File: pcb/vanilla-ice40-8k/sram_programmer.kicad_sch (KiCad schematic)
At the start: 43 parts, among them J10 Conn_01x05_Pin, J9 Conn_01x06_Pin, U2 W25X40CLSN, U3 FT2232HL, U4 93LCxxBxxOT, Y1 12Mhz/18pf

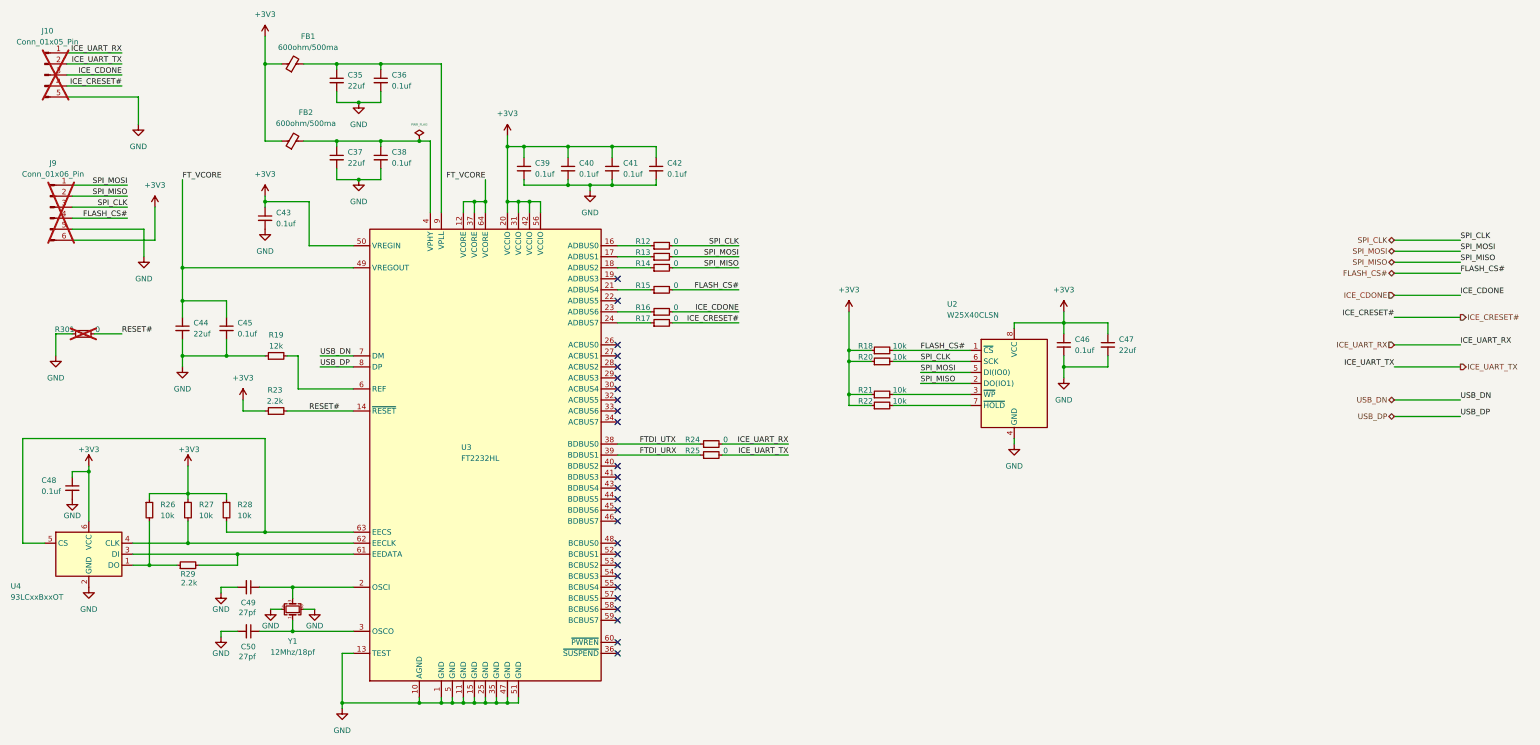
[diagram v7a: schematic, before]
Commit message: [hx8k][pcb] start of rough layout
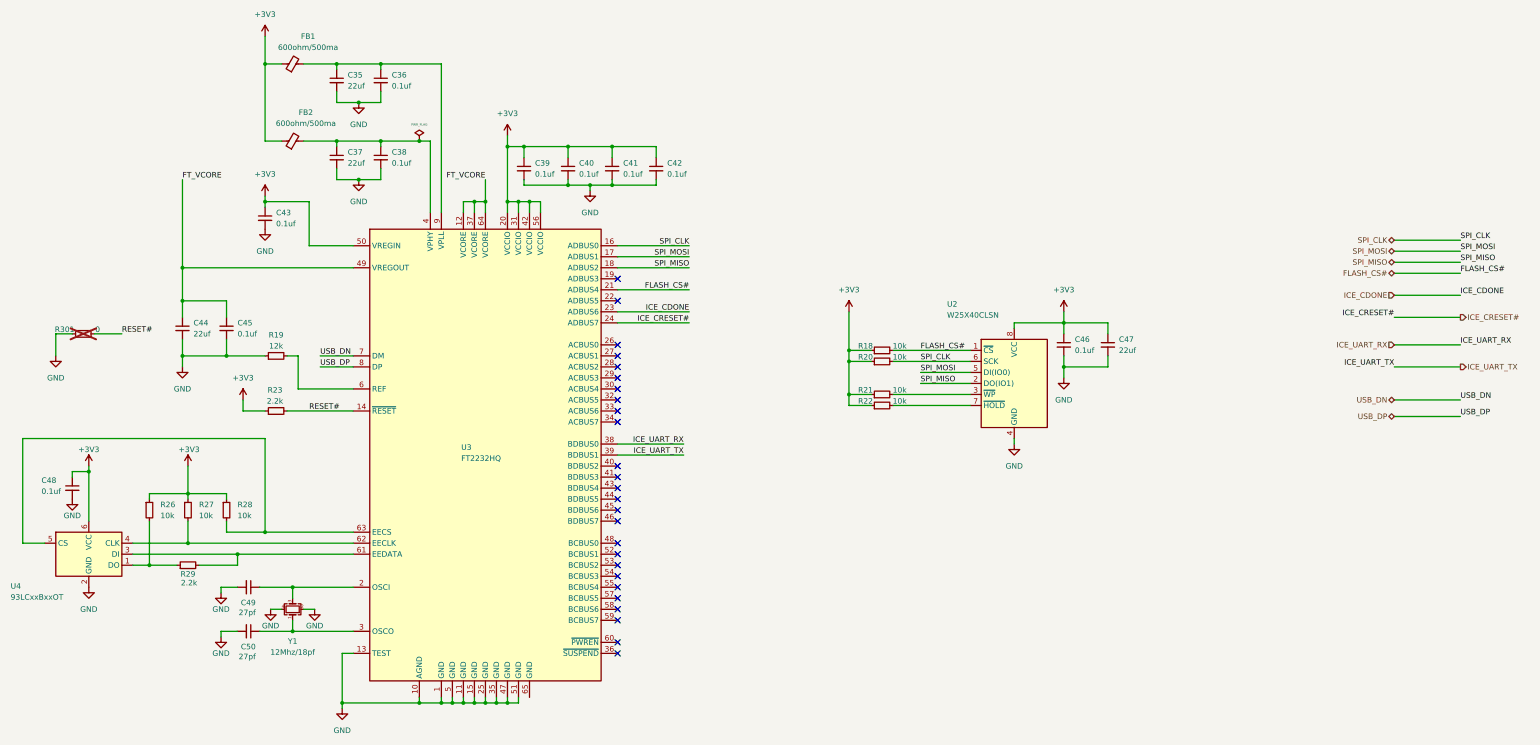
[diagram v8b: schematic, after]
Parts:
- removed J10: Conn_01x05_Pin, Connector_PinHeader_2.54mm:PinHeader_1x05_P2.54mm_Vertical, symbol Connector:Conn_01x05_Pin
- removed J9: Conn_01x06_Pin, Connector_PinHeader_2.54mm:PinHeader_1x06_P2.54mm_Vertical, symbol Connector:Conn_01x06_Pin
- removed R12, R13, R14, R15, R16, R17, R24, R25: 0, Resistor_SMD:R_0603_1608Metric, symbol Device:R_Small
- U3: value FT2232HL -> FT2232HQ; footprint Package_QFP:LQFP-64_10x10mm_P0.5mm -> !Misc:FT2232HQ; symbol Interface_USB:FT2232HL -> !Misc:FT2232HQ; Digi-Key Part Number 768-1024-1-ND -> 768-1025-1-ND; LCSC Part # C27882 -> C193662
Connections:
- net FTDI_URX is gone; now on net ICE_UART_TX: U3.39 (BDBUS1)
- net FTDI_UTX is gone; now on net ICE_UART_RX: U3.38 (BDBUS0)
- net FLASH_CS#: now also U3.21 (ADBUS4)
- net ICE_CDONE: now also U3.23 (ADBUS6)
- net ICE_CRESET#: now also U3.24 (ADBUS7)
- net SPI_CLK: now also U3.16 (ADBUS0)
- net SPI_MISO: now also U3.18 (ADBUS2)
- net SPI_MOSI: now also U3.17 (ADBUS1)
